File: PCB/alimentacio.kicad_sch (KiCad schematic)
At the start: 17 parts, among them J1 PowerIN, U1 LT1528CT-PBF

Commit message: changed clks, pwr
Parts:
- C1, C2: footprint (none) -> Capacitor_SMD:C_0805_2012Metric
- C3, C4, C5, C6: footprint (none) -> Capacitor_THT:CP_Radial_D5.0mm_P2.00mm
- R_LDO1: renamed from R2; footprint (none) -> Resistor_SMD:R_0805_2012Metric_Pad1.20x1.40mm_HandSolder
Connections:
- net GND: no longer C33.2
- net GNDPWR: now also C33.2
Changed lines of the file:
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@@
     (pin "1")
     (instances
-      (project "alimentacio"
-        (path "/88fa5da0-8701-4b36-a7b6-c9dab3428a53"
+      (project "DIJOUS_4_PORTES"
+        (path "/69b34976-047e-478e-bd76-9b6ef0dba356/0e58b9bb-7a32-4563-ae50-f5e325ba8348"
           (reference "#PWR03") (unit 1)
         )
       )
+      (project "alimentacio"
+        (path "/88fa5da0-8701-4b36-a7b6-c9dab3428a53"
+          (reference "#PWR03") (unit 1)
+        )
+      )
     )
   )
@@
   (symbol (lib_id "Device:R") (at 233.68 58.42 180) (unit 1)
     (in_bom yes) (on_board yes) (dnp no)
-    (property "Reference" "R2" (at 229.87 58.42 0)
+    (property "Reference" "R_LDO1" (at 229.87 58.42 90)
       (effects (font (size 1.27 1.27)))
     )
@@
       (effects (font (size 1.27 1.27)))
     )
-    (property "Footprint" "" (at 235.458 58.42 90)
+    (property "Footprint" "Resistor_SMD:R_0805_2012Metric_Pad1.20x1.40mm_HandSolder" (at 235.458 58.42 90)
       (effects (font (size 1.27 1.27)) hide)
     )
@@
       (project "DIJOUS_4_PORTES"
         (path "/69b34976-047e-478e-bd76-9b6ef0dba356/0e58b9bb-7a32-4563-ae50-f5e325ba8348"
+          (reference "R_LDO1") (unit 1)
+        )
+      )
+      (project "alimentacio"
+        (path "/88fa5da0-8701-4b36-a7b6-c9dab3428a53"
           (reference "R2") (unit 1)
         )
       )
-      (project "alimentacio"
-        (path "/88fa5da0-8701-4b36-a7b6-c9dab3428a53"
-          (reference "R2") (unit 1)
-        )
-      )
     )
   )
@@
         (path "/88fa5da0-8701-4b36-a7b6-c9dab3428a53"
           (reference "#PWR04") (unit 1)
+        )
+      )
+    )
+  )
+  (symbol (lib_id "power:GNDPWR") (at 140.97 62.23 0) (unit 1)
+    (in_bom yes) (on_board yes) (dnp no)
+    (property "Reference" "#PWR057" (at 140.97 67.31 0)
+      (effects (font (size 1.27 1.27)) hide)
+    )
+    (property "Value" "GNDPWR" (at 140.97 66.04 0)
+      (effects (font (size 1.27 1.27)))
+    )
+    (property "Footprint" "" (at 140.97 63.5 0)
+      (effects (font (size 1.27 1.27)) hide)
+    )
+    (property "Datasheet" "" (at 140.97 63.5 0)
+      (effects (font (size 1.27 1.27)) hide)
+    )
+    (pin "1")
+    (instances
+      (project "DIJOUS_4_PORTES"
+        (path "/69b34976-047e-478e-bd76-9b6ef0dba356/0e58b9bb-7a32-4563-ae50-f5e325ba8348"
+          (reference "#PWR057") (unit 1)
+        )
+      )
+      (project "alimentacio"
+        (path "/88fa5da0-8701-4b36-a7b6-c9dab3428a53"
+          (reference "#PWR055") (unit 1)
         )
       )
@@
   (symbol (lib_id "power:+3.3V") (at 270.51 41.91 0) (unit 1)
     (in_bom yes) (on_board yes) (dnp no) (fields_autoplaced)
-    (property "Reference" "#PWR03" (at 270.51 45.72 0)
+    (property "Reference" "#PWR0101" (at 270.51 45.72 0)
       (effects (font (size 1.27 1.27)) hide)
     )
@@
       (project "DIJOUS_4_PORTES"
         (path "/69b34976-047e-478e-bd76-9b6ef0dba356/0e58b9bb-7a32-4563-ae50-f5e325ba8348"
-          (reference "#PWR03") (unit 1)
+          (reference "#PWR0101") (unit 1)
         )
       )
@@
     (pin "1")
     (instances
-      (project "alimentacio"
-        (path "/88fa5da0-8701-4b36-a7b6-c9dab3428a53"
+      (project "DIJOUS_4_PORTES"
+        (path "/69b34976-047e-478e-bd76-9b6ef0dba356/0e58b9bb-7a32-4563-ae50-f5e325ba8348"
           (reference "#PWR010") (unit 1)
         )
       )
+      (project "alimentacio"
+        (path "/88fa5da0-8701-4b36-a7b6-c9dab3428a53"
+          (reference "#PWR010") (unit 1)
+        )
+      )
     )
   )
@@
       (effects (font (size 1.27 1.27)) (justify left))
     )
-    (property "Footprint" "" (at 174.9552 57.15 0)
+    (property "Footprint" "Capacitor_SMD:C_0805_2012Metric" (at 174.9552 57.15 0)
       (effects (font (size 1.27 1.27)) hide)
     )
@@
       (effects (font (size 1.27 1.27)) (justify left))
     )
-    (property "Footprint" "" (at 252.73 57.15 0)
+    (property "Footprint" "Capacitor_THT:CP_Radial_D5.0mm_P2.00mm" (at 252.73 57.15 0)
       (effects (font (size 1.27 1.27)) hide)
     )
@@
       (effects (font (size 1.27 1.27)) (justify left))
     )
-    (property "Footprint" "" (at 243.84 57.15 0)
+    (property "Footprint" "Capacitor_THT:CP_Radial_D5.0mm_P2.00mm" (at 243.84 57.15 0)
       (effects (font (size 1.27 1.27)) hide)
     )
@@
         (path "/88fa5da0-8701-4b36-a7b6-c9dab3428a53"
           (reference "C3") (unit 1)
-        )
-      )
-    )
-  )
-  (symbol (lib_id "power:GND") (at 140.97 62.23 0) (unit 1)
-    (in_bom yes) (on_board yes) (dnp no)
-    (property "Reference" "#PWR058" (at 140.97 68.58 0)
-      (effects (font (size 1.27 1.27)) hide)
-    )
-    (property "Value" "GND" (at 140.97 66.04 0)
-      (effects (font (size 1.27 1.27)))
-    )
-    (property "Footprint" "" (at 140.97 62.23 0)
-      (effects (font (size 1.27 1.27)) hide)
-    )
-    (property "Datasheet" "" (at 140.97 62.23 0)
-      (effects (font (size 1.27 1.27)) hide)
-    )
-    (pin "1")
-    (instances
-      (project "DIJOUS_4_PORTES"
-        (path "/69b34976-047e-478e-bd76-9b6ef0dba356/0e58b9bb-7a32-4563-ae50-f5e325ba8348"
-          (reference "#PWR058") (unit 1)
-        )
-      )
-      (project "alimentacio"
-        (path "/88fa5da0-8701-4b36-a7b6-c9dab3428a53"
-          (reference "#PWR058") (unit 1)
         )
       )
@@
       (effects (font (size 1.27 1.27)) (justify left))
     )
-    (property "Footprint" "" (at 261.62 57.15 0)
+    (property "Footprint" "Capacitor_THT:CP_Radial_D5.0mm_P2.00mm" (at 261.62 57.15 0)
       (effects (font (size 1.27 1.27)) hide)
     )
@@
       (effects (font (size 1.27 1.27)) (justify left))
     )
-    (property "Footprint" "" (at 181.3052 57.15 0)
+    (property "Footprint" "Capacitor_SMD:C_0805_2012Metric" (at 181.3052 57.15 0)
       (effects (font (size 1.27 1.27)) hide)
     )
@@
       (effects (font (size 1.27 1.27)) (justify left))
     )
-    (property "Footprint" "" (at 270.51 57.15 0)
-      (effects (font (size 1.27 1.27)) hide)
-    )
+    (property "Footprint" "Capacitor_THT:CP_Radial_D5.0mm_P2.00mm" (at 270.51 57.15 0)
+      (effects (font (size 1.27 1.27)) hide)
+    )

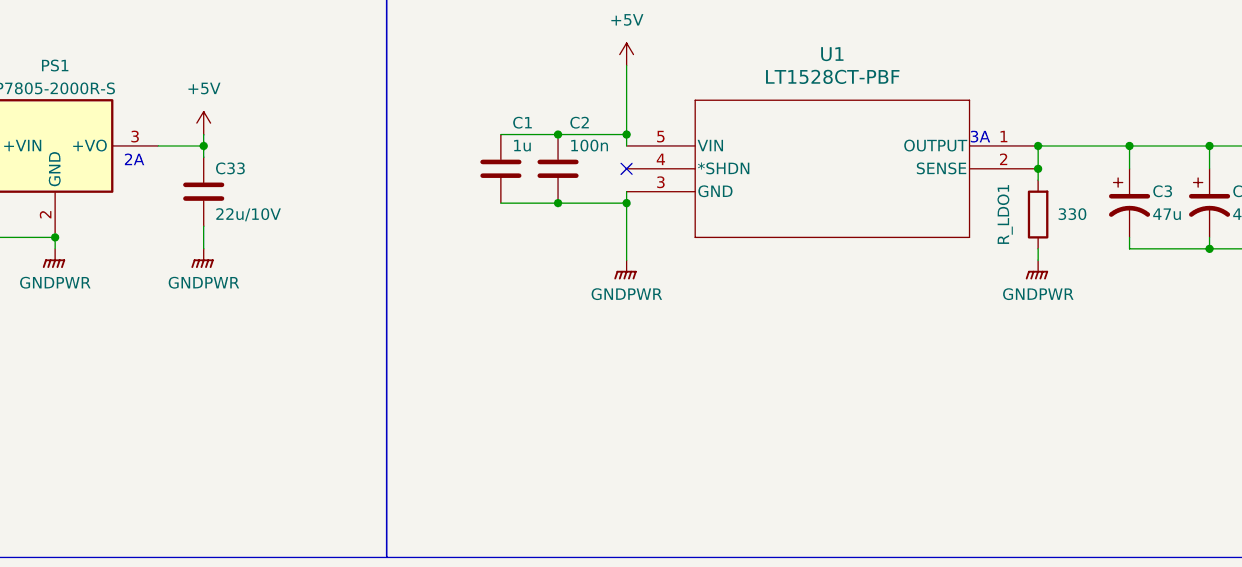
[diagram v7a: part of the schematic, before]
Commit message: Netclasses Layout i canvis de GNDPWR a GND al layout d'alimentació
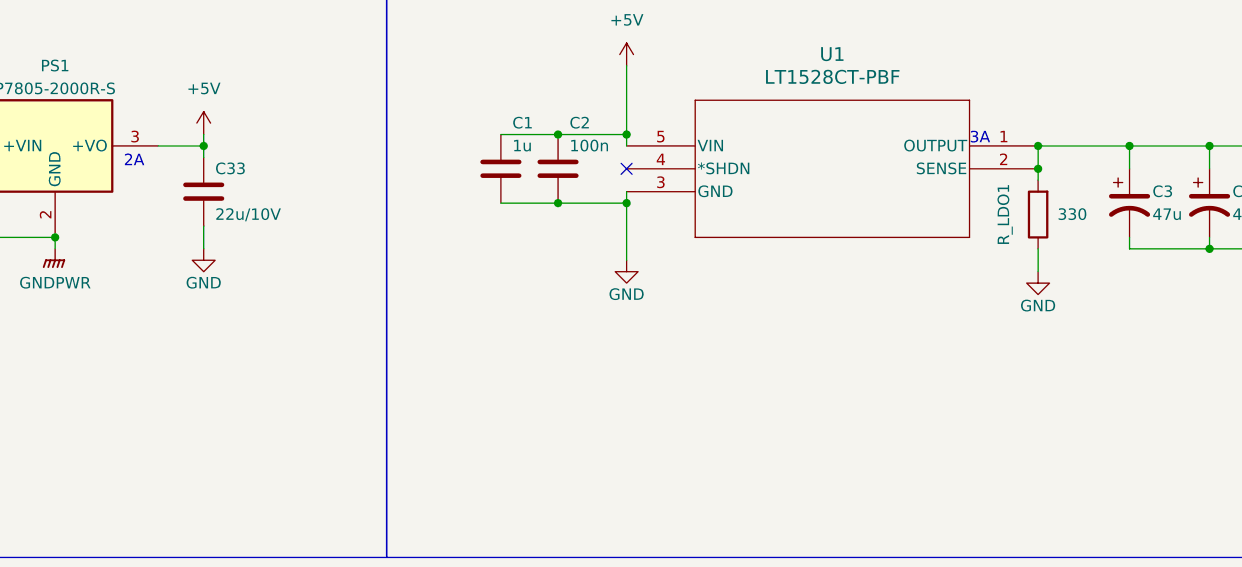
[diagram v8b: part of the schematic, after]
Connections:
- net GND: now also C1.2, C2.2, C33.2, R_LDO1.1, U1.3 (GND)
- net GNDPWR: no longer C1.2, C2.2, C33.2, R_LDO1.1, U1.3 (GND)
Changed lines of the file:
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@@
     (stroke (width 0) (type default))
   )
-  (wire (pts (xy 233.68 63.5) (xy 233.68 62.23))
+  (wire (pts (xy 233.68 64.77) (xy 233.68 62.23))
     (stroke (width 0) (type default))
   )
@@
     )
   )
-  (symbol (lib_id "power:GNDPWR") (at 187.96 63.5 0) (unit 1)
-    (in_bom yes) (on_board yes) (dnp no)
-    (property "Reference" "#PWR08" (at 187.96 68.58 0)
-      (effects (font (size 1.27 1.27)) hide)
-    )
-    (property "Value" "GNDPWR" (at 187.96 67.31 0)
-      (effects (font (size 1.27 1.27)))
-    )
-    (property "Footprint" "" (at 187.96 64.77 0)
-      (effects (font (size 1.27 1.27)) hide)
-    )
-    (property "Datasheet" "" (at 187.96 64.77 0)
-      (effects (font (size 1.27 1.27)) hide)
-    )
-    (pin "1")
-    (instances
-      (project "DIJOUS_4_PORTES"
-        (path "/69b34976-047e-478e-bd76-9b6ef0dba356/0e58b9bb-7a32-4563-ae50-f5e325ba8348"
-          (reference "#PWR08") (unit 1)
-        )
-      )
-      (project "alimentacio"
-        (path "/88fa5da0-8701-4b36-a7b6-c9dab3428a53"
-          (reference "#PWR04") (unit 1)
-        )
-      )
-    )
-  )
-  (symbol (lib_id "power:GNDPWR") (at 140.97 62.23 0) (unit 1)
-    (in_bom yes) (on_board yes) (dnp no)
-    (property "Reference" "#PWR057" (at 140.97 67.31 0)
-      (effects (font (size 1.27 1.27)) hide)
-    )
-    (property "Value" "GNDPWR" (at 140.97 66.04 0)
-      (effects (font (size 1.27 1.27)))
-    )
-    (property "Footprint" "" (at 140.97 63.5 0)
-      (effects (font (size 1.27 1.27)) hide)
-    )
-    (property "Datasheet" "" (at 140.97 63.5 0)
-      (effects (font (size 1.27 1.27)) hide)
-    )
-    (pin "1")
-    (instances
-      (project "DIJOUS_4_PORTES"
-        (path "/69b34976-047e-478e-bd76-9b6ef0dba356/0e58b9bb-7a32-4563-ae50-f5e325ba8348"
-          (reference "#PWR057") (unit 1)
-        )
-      )
-      (project "alimentacio"
-        (path "/88fa5da0-8701-4b36-a7b6-c9dab3428a53"
-          (reference "#PWR055") (unit 1)
-        )
-      )
-    )
-  )
   (symbol (lib_id "P7803-2000R-S:P7803-2000R-S") (at 113.03 48.26 0) (unit 1)
     (in_bom yes) (on_board yes) (dnp no)
@@
     )
   )
-  (symbol (lib_id "power:GNDPWR") (at 233.68 63.5 0) (unit 1)
-    (in_bom yes) (on_board yes) (dnp no)
-    (property "Reference" "#PWR07" (at 233.68 68.58 0)
-      (effects (font (size 1.27 1.27)) hide)
-    )
-    (property "Value" "GNDPWR" (at 233.68 67.31 0)
-      (effects (font (size 1.27 1.27)))
-    )
-    (property "Footprint" "" (at 233.68 64.77 0)
-      (effects (font (size 1.27 1.27)) hide)
-    )
-    (property "Datasheet" "" (at 233.68 64.77 0)
-      (effects (font (size 1.27 1.27)) hide)
-    )
-    (pin "1")
-    (instances
-      (project "DIJOUS_4_PORTES"
-        (path "/69b34976-047e-478e-bd76-9b6ef0dba356/0e58b9bb-7a32-4563-ae50-f5e325ba8348"
-          (reference "#PWR07") (unit 1)
-        )
-      )
-      (project "alimentacio"
-        (path "/88fa5da0-8701-4b36-a7b6-c9dab3428a53"
-          (reference "#PWR07") (unit 1)
-        )
-      )
-    )
-  )
   (symbol (lib_id "power:+5V") (at 140.97 49.53 0) (unit 1)
     (in_bom yes) (on_board yes) (dnp no) (fields_autoplaced)
@@
         (path "/88fa5da0-8701-4b36-a7b6-c9dab3428a53"
           (reference "#PWR043") (unit 1)
+        )
+      )
+    )
+  )
+  (symbol (lib_id "power:GND") (at 187.96 63.5 0) (unit 1)
+    (in_bom yes) (on_board yes) (dnp no)
+    (property "Reference" "#PWR059" (at 187.96 69.85 0)
+      (effects (font (size 1.27 1.27)) hide)
+    )
+    (property "Value" "GND" (at 187.96 67.31 0)
+      (effects (font (size 1.27 1.27)))
+    )
+    (property "Footprint" "" (at 187.96 63.5 0)
+      (effects (font (size 1.27 1.27)) hide)
+    )
+    (property "Datasheet" "" (at 187.96 63.5 0)
+      (effects (font (size 1.27 1.27)) hide)
+    )
+    (pin "1")
+    (instances
+      (project "DIJOUS_4_PORTES"
+        (path "/69b34976-047e-478e-bd76-9b6ef0dba356/0e58b9bb-7a32-4563-ae50-f5e325ba8348"
+          (reference "#PWR059") (unit 1)
         )
       )
@@
     )
   )
+  (symbol (lib_id "power:GND") (at 140.97 62.23 0) (unit 1)
+    (in_bom yes) (on_board yes) (dnp no)
+    (property "Reference" "#PWR07" (at 140.97 68.58 0)
+      (effects (font (size 1.27 1.27)) hide)
+    )
+    (property "Value" "GND" (at 140.97 66.04 0)
+      (effects (font (size 1.27 1.27)))
+    )
+    (property "Footprint" "" (at 140.97 62.23 0)
+      (effects (font (size 1.27 1.27)) hide)
+    )
+    (property "Datasheet" "" (at 140.97 62.23 0)
+      (effects (font (size 1.27 1.27)) hide)
+    )
+    (pin "1")
+    (instances
+      (project "DIJOUS_4_PORTES"
+        (path "/69b34976-047e-478e-bd76-9b6ef0dba356/0e58b9bb-7a32-4563-ae50-f5e325ba8348"
+          (reference "#PWR07") (unit 1)
+        )
+      )
+    )
+  )
   (symbol (lib_id "Device:D_Zener") (at 46.99 57.15 270) (unit 1)
     (in_bom yes) (on_board yes) (dnp no)
@@
         )
       )
+    )
+  )
+  (symbol (lib_id "power:GND") (at 233.68 64.77 0) (unit 1)
+    (in_bom yes) (on_board yes) (dnp no)
+    (property "Reference" "#PWR061" (at 233.68 71.12 0)
+      (effects (font (size 1.27 1.27)) hide)
+    )
+    (property "Value" "GND" (at 233.68 68.58 0)
+      (effects (font (size 1.27 1.27)))
+    )
+    (property "Footprint" "" (at 233.68 64.77 0)
+      (effects (font (size 1.27 1.27)) hide)
+    )
+    (property "Datasheet" "" (at 233.68 64.77 0)
+      (effects (font (size 1.27 1.27)) hide)
+    )
+    (pin "1")
+    (instances
+      (project "DIJOUS_4_PORTES"
+        (path "/69b34976-047e-478e-bd76-9b6ef0dba356/0e58b9bb-7a32-4563-ae50-f5e325ba8348"
+          (reference "#PWR061") (unit 1)
+        )
+      )
